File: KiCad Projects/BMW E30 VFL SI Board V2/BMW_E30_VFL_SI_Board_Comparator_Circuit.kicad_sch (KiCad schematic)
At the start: 39 parts, among them K1 SR7-9V-200-1C, Q1 BC547C, U2 LM2901

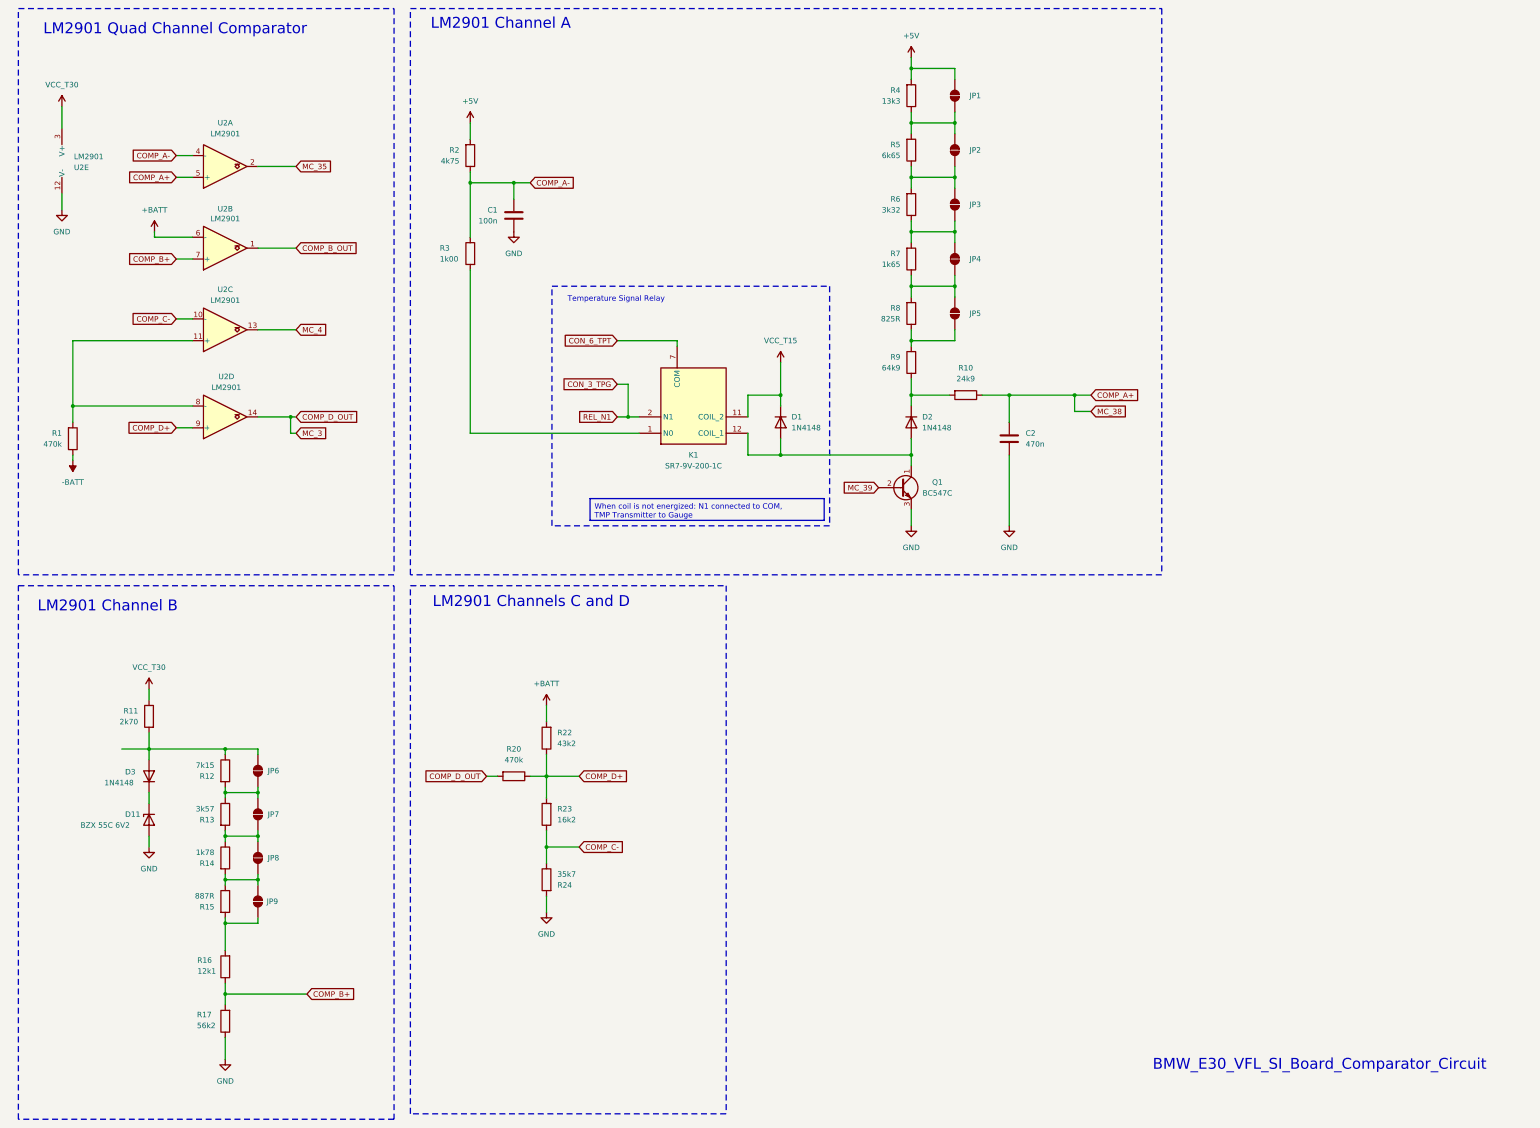
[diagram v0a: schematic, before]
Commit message: Bugfixing of component designators
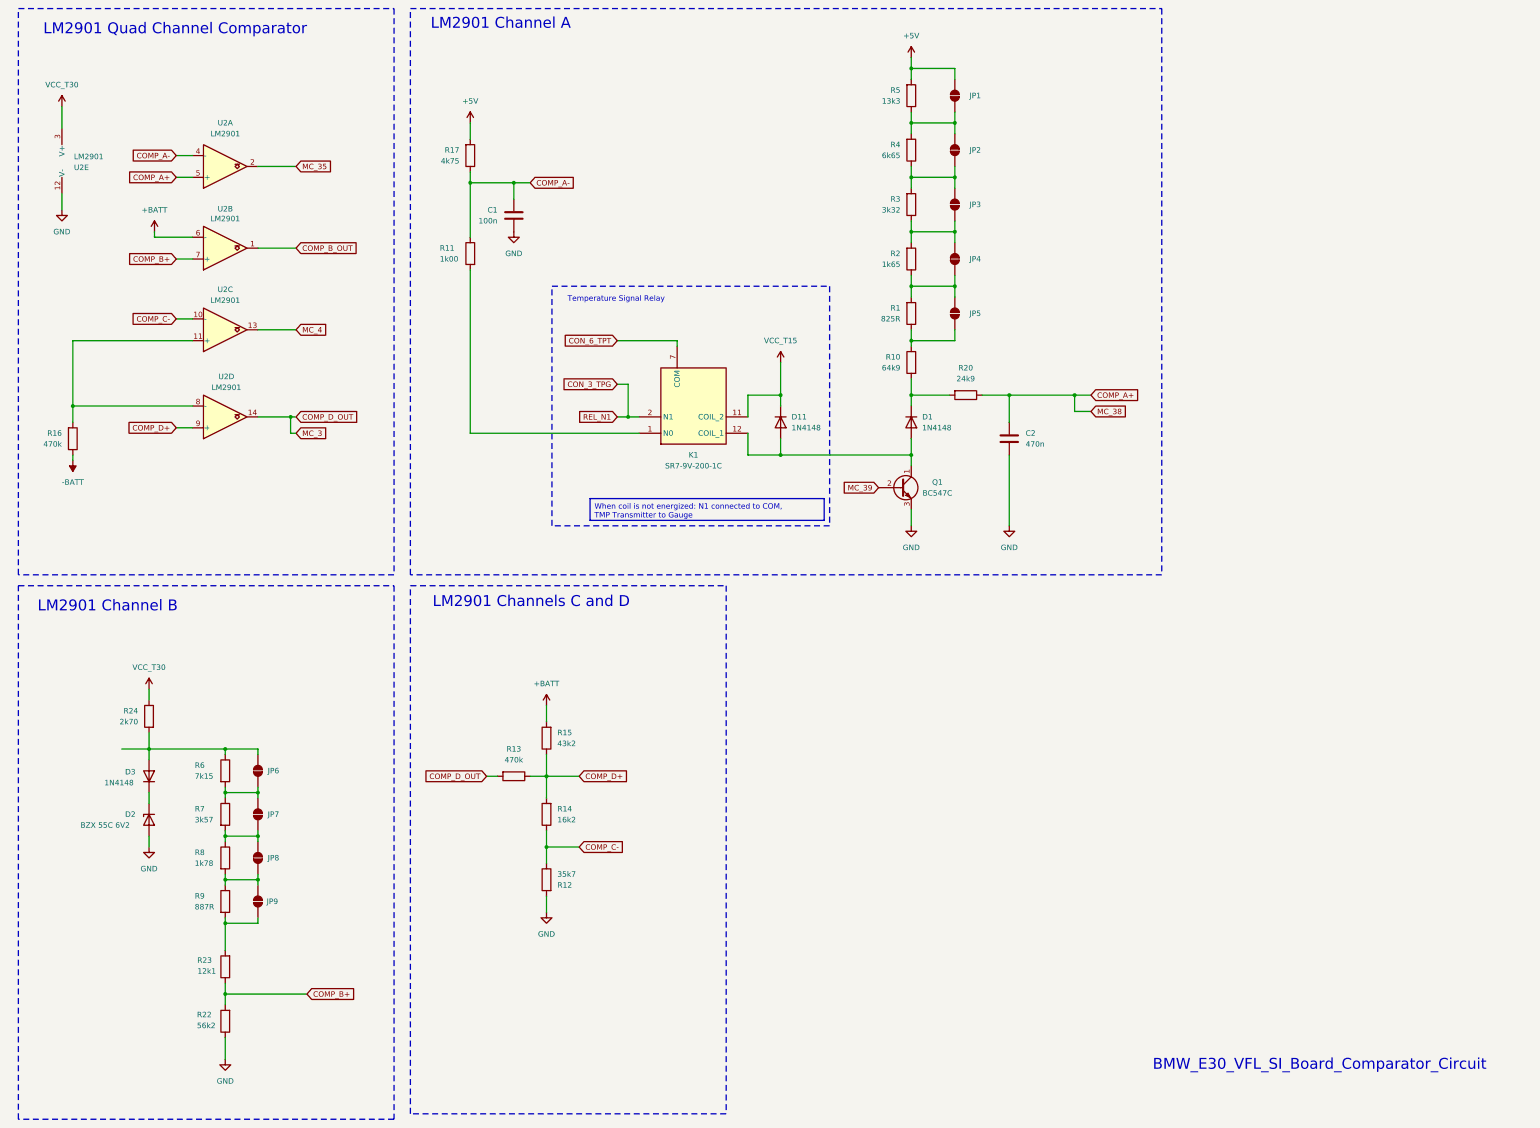
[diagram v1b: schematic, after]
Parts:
- renumbered D2 to D1, D1 to D11, D11 to D2, R8 to R1, R9 to R10, R3 to R11, R24 to R12, R20 to R13, R23 to R14, R22 to R15, R1 to R16, R2 to R17, R7 to R2, R10 to R20, R17 to R22, R16 to R23, R11 to R24, R6 to R3, R5 to R4, R4 to R5, R12 to R6, R13 to R7, R14 to R8, R15 to R9
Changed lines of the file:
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@@
 		(dnp no)
 		(fields_autoplaced yes)
-		(property "Reference" "R5"
+		(property "Reference" "R4"
 			(at 252.73 46.9899 0)
 			(effects
@@
 			(project "BMW E30 VFL SI Board V2"
 				(path "/b9f8b657-f23f-4f46-b33b-c9c07ea00dca/c70e424d-af87-4480-9570-0fdeb437e545"
-					(reference "R5")
+					(reference "R4")
 					(unit 1)
 				)
@@
 		(dnp no)
 		(fields_autoplaced yes)
-		(property "Reference" "D2"
+		(property "Reference" "D1"
 			(at 257.81 110.4899 90)
 			(effects
@@
 			(project "BMW E30 VFL SI Board V2"
 				(path "/b9f8b657-f23f-4f46-b33b-c9c07ea00dca/c70e424d-af87-4480-9570-0fdeb437e545"
-					(reference "D2")
+					(reference "D1")
 					(unit 1)
 				)
@@
 		(on_board yes)
 		(dnp no)
-		(property "Reference" "R24"
+		(property "Reference" "R12"
 			(at 172.72 219.7101 0)
 			(effects
@@
 			(project "BMW E30 VFL SI Board V2"
 				(path "/b9f8b657-f23f-4f46-b33b-c9c07ea00dca/c70e424d-af87-4480-9570-0fdeb437e545"
-					(reference "R24")
+					(reference "R12")
 					(unit 1)
 				)
@@
 		(dnp no)
 		(fields_autoplaced yes)
-		(property "Reference" "R8"
+		(property "Reference" "R1"
 			(at 252.73 85.0899 0)
 			(effects
@@
 			(project "BMW E30 VFL SI Board V2"
 				(path "/b9f8b657-f23f-4f46-b33b-c9c07ea00dca/c70e424d-af87-4480-9570-0fdeb437e545"
-					(reference "R8")
+					(reference "R1")
 					(unit 1)
 				)
@@
 		(dnp no)
 		(fields_autoplaced yes)
-		(property "Reference" "R20"
+		(property "Reference" "R13"
 			(at 162.56 187.96 90)
 			(effects
@@
 			(project "BMW E30 VFL SI Board V2"
 				(path "/b9f8b657-f23f-4f46-b33b-c9c07ea00dca/c70e424d-af87-4480-9570-0fdeb437e545"
-					(reference "R20")
+					(reference "R13")
 					(unit 1)
 				)
@@
 		(dnp no)
 		(fields_autoplaced yes)
-		(property "Reference" "R6"
+		(property "Reference" "R3"
 			(at 252.73 59.6899 0)
 			(effects
@@
 			(project "BMW E30 VFL SI Board V2"
 				(path "/b9f8b657-f23f-4f46-b33b-c9c07ea00dca/c70e424d-af87-4480-9570-0fdeb437e545"
-					(reference "R6")
+					(reference "R3")
 					(unit 1)
 				)
@@
 		(dnp no)
 		(fields_autoplaced yes)
-		(property "Reference" "R22"
+		(property "Reference" "R15"
 			(at 172.72 184.1499 0)
 			(effects
@@
 			(project "BMW E30 VFL SI Board V2"
 				(path "/b9f8b657-f23f-4f46-b33b-c9c07ea00dca/c70e424d-af87-4480-9570-0fdeb437e545"
-					(reference "R22")
+					(reference "R15")
 					(unit 1)
 				)
@@
 		(on_board yes)
 		(dnp no)
-		(property "Reference" "R9"
+		(property "Reference" "R10"
 			(at 252.73 96.5199 0)
 			(effects
@@
 			(project "BMW E30 VFL SI Board V2"
 				(path "/b9f8b657-f23f-4f46-b33b-c9c07ea00dca/c70e424d-af87-4480-9570-0fdeb437e545"
-					(reference "R9")
+					(reference "R10")
 					(unit 1)
 				)
@@
 		(on_board yes)
 		(dnp no)
-		(fields_autoplaced yes)
-		(property "Reference" "R12"
-			(at 92.71 194.3101 0)
+		(property "Reference" "R6"
+			(at 88.138 191.77 0)
 			(effects
 				(font
 					(size 1.27 1.27)
 				)
-				(justify right)
+				(justify left)
 			)
 		)
 		(property "Value" "7k15"
-			(at 92.71 191.7701 0)
+			(at 88.138 194.31 0)
 			(effects
 				(font
 					(size 1.27 1.27)
 				)
-				(justify right)
+				(justify left)
 			)
 		)
@@
 			(project "BMW E30 VFL SI Board V2"
 				(path "/b9f8b657-f23f-4f46-b33b-c9c07ea00dca/c70e424d-af87-4480-9570-0fdeb437e545"
-					(reference "R12")
+					(reference "R6")
 					(unit 1)
 				)
@@
 		(on_board yes)
 		(dnp no)
-		(property "Reference" "R3"
+		(property "Reference" "R11"
 			(at 145.288 71.12 0)
 			(effects
@@
 			(project "BMW E30 VFL SI Board V2"
 				(path "/b9f8b657-f23f-4f46-b33b-c9c07ea00dca/c70e424d-af87-4480-9570-0fdeb437e545"
-					(reference "R3")
+					(reference "R11")
 					(unit 1)
 				)
@@
 		(on_board yes)
 		(dnp no)
-		(fields_autoplaced yes)
-		(property "Reference" "R11"
+		(property "Reference" "R24"
 			(at 74.93 179.0699 0)
 			(effects
@@
 			(project "BMW E30 VFL SI Board V2"
 				(path "/b9f8b657-f23f-4f46-b33b-c9c07ea00dca/c70e424d-af87-4480-9570-0fdeb437e545"
-					(reference "R11")
+					(reference "R24")
 					(unit 1)
 				)
@@
 		(dnp no)
 		(fields_autoplaced yes)
-		(property "Reference" "R23"
+		(property "Reference" "R14"
 			(at 172.72 201.9299 0)
 			(effects
@@
 			(project "BMW E30 VFL SI Board V2"
 				(path "/b9f8b657-f23f-4f46-b33b-c9c07ea00dca/c70e424d-af87-4480-9570-0fdeb437e545"
-					(reference "R23")
+					(reference "R14")
 					(unit 1)
 				)
@@
 		(dnp no)
 		(fields_autoplaced yes)
-		(property "Reference" "R1"
+		(property "Reference" "R16"
 			(at 57.15 114.2999 0)
 			(effects
@@
 			(project "BMW E30 VFL SI Board V2"
 				(path "/b9f8b657-f23f-4f46-b33b-c9c07ea00dca/c70e424d-af87-4480-9570-0fdeb437e545"
-					(reference "R1")
+					(reference "R16")
 					(unit 1)
 				)
@@
 		(on_board yes)
 		(dnp no)
-		(fields_autoplaced yes)
-		(property "Reference" "R13"
-			(at 92.71 204.4701 0)
+		(property "Reference" "R7"
+			(at 88.138 201.93 0)
 			(effects
 				(font
 					(size 1.27 1.27)
 				)
-				(justify right)
+				(justify left)
 			)
 		)
 		(property "Value" "3k57"
-			(at 92.71 201.9301 0)
+			(at 88.138 204.47 0)
 			(effects
 				(font
 					(size 1.27 1.27)
 				)
-				(justify right)
+				(justify left)
 			)
 		)
@@
 			(project "BMW E30 VFL SI Board V2"
 				(path "/b9f8b657-f23f-4f46-b33b-c9c07ea00dca/c70e424d-af87-4480-9570-0fdeb437e545"
-					(reference "R13")
+					(reference "R7")
 					(unit 1)
 				)
@@
 		(dnp no)
 		(fields_autoplaced yes)
-		(property "Reference" "D1"
+		(property "Reference" "D11"
 			(at 227.33 110.4899 90)
 			(effects
@@
 			(project "BMW E30 VFL SI Board V2"
 				(path "/b9f8b657-f23f-4f46-b33b-c9c07ea00dca/c70e424d-af87-4480-9570-0fdeb437e545"
-					(reference "D1")
+					(reference "D11")
 					(unit 1)
 				)
@@
 		(on_board yes)
 		(dnp no)
-		(property "Reference" "R17"
+		(property "Reference" "R22"
 			(at 88.646 249.936 0)
 			(effects
@@
 			(project "BMW E30 VFL SI Board V2"
 				(path "/b9f8b657-f23f-4f46-b33b-c9c07ea00dca/c70e424d-af87-4480-9570-0fdeb437e545"
-					(reference "R17")
+					(reference "R22")
 					(unit 1)
 				)
@@
 		(on_board yes)
 		(dnp no)
-		(property "Reference" "D11"
+		(property "Reference" "D2"
 			(at 71.882 203.2 90)
 			(effects
@@
 			(project "BMW E30 VFL SI Board V2"
 				(path "/b9f8b657-f23f-4f46-b33b-c9c07ea00dca/c70e424d-af87-4480-9570-0fdeb437e545"
-					(reference "D11")
+					(reference "D2")
 					(unit 1)
 				)
@@
 		(dnp no)
 		(fields_autoplaced yes)
-		(property "Reference" "R7"
+		(property "Reference" "R2"
 			(at 252.73 72.3899 0)
 			(effects
@@
 			(project "BMW E30 VFL SI Board V2"
 				(path "/b9f8b657-f23f-4f46-b33b-c9c07ea00dca/c70e424d-af87-4480-9570-0fdeb437e545"
-					(reference "R7")
+					(reference "R2")
 					(unit 1)
 				)
@@
 		(on_board yes)
 		(dnp no)
-		(fields_autoplaced yes)
-		(property "Reference" "R15"
-			(at 92.71 224.7901 0)
+		(property "Reference" "R9"
+			(at 88.138 222.25 0)
 			(effects
 				(font
 					(size 1.27 1.27)
 				)
-				(justify right)
+				(justify left)
 			)
 		)
 		(property "Value" "887R"
-			(at 92.71 222.2501 0)
+			(at 88.138 224.79 0)
 			(effects
 				(font
 					(size 1.27 1.27)
 				)
-				(justify right)
+				(justify left)
 			)
 		)
@@
 			(project "BMW E30 VFL SI Board V2"
 				(path "/b9f8b657-f23f-4f46-b33b-c9c07ea00dca/c70e424d-af87-4480-9570-0fdeb437e545"
-					(reference "R15")
+					(reference "R9")
 					(unit 1)
 				)
@@
 		(dnp no)
 		(fields_autoplaced yes)
-		(property "Reference" "R4"
+		(property "Reference" "R5"
 			(at 252.73 34.2899 0)
 			(effects
@@
 			(project "BMW E30 VFL SI Board V2"
 				(path "/b9f8b657-f23f-4f46-b33b-c9c07ea00dca/c70e424d-af87-4480-9570-0fdeb437e545"
-					(reference "R4")
+					(reference "R5")
 					(unit 1)
 				)
@@
 		(dnp no)
 		(fields_autoplaced yes)
-		(property "Reference" "R2"
+		(property "Reference" "R17"
 			(at 149.86 48.2599 0)
 			(effects
@@
 			(project "BMW E30 VFL SI Board V2"
 				(path "/b9f8b657-f23f-4f46-b33b-c9c07ea00dca/c70e424d-af87-4480-9570-0fdeb437e545"
-					(reference "R2")
+					(reference "R17")
 					(unit 1)
 				)
@@
 		(on_board yes)
 		(dnp no)
-		(property "Reference" "R16"
+		(property "Reference" "R23"
 			(at 90.424 237.236 0)
 			(effects
@@
 			(project "BMW E30 VFL SI Board V2"
 				(path "/b9f8b657-f23f-4f46-b33b-c9c07ea00dca/c70e424d-af87-4480-9570-0fdeb437e545"
-					(reference "R16")
+					(reference "R23")
 					(unit 1)
 				)
@@
 		(on_board yes)
 		(dnp no)
-		(fields_autoplaced yes)
-		(property "Reference" "R14"
-			(at 92.71 214.6301 0)
+		(property "Reference" "R8"
+			(at 88.138 212.09 0)
 			(effects
 				(font
 					(size 1.27 1.27)
 				)
-				(justify right)
+				(justify left)
 			)
 		)
 		(property "Value" "1k78"
-			(at 92.71 212.0901 0)
+			(at 88.138 214.63 0)
 			(effects
 				(font
 					(size 1.27 1.27)
 				)
-				(justify right)
+				(justify left)
 			)
 		)
@@
 			(project "BMW E30 VFL SI Board V2"
 				(path "/b9f8b657-f23f-4f46-b33b-c9c07ea00dca/c70e424d-af87-4480-9570-0fdeb437e545"
-					(reference "R14")
+					(reference "R8")
 					(unit 1)
 				)
@@
 		(dnp no)
 		(fields_autoplaced yes)
-		(property "Reference" "R10"
+		(property "Reference" "R20"
 			(at 267.97 99.06 90)
 			(effects
@@
 			(project "BMW E30 VFL SI Board V2"
 				(path "/b9f8b657-f23f-4f46-b33b-c9c07ea00dca/c70e424d-af87-4480-9570-0fdeb437e545"
-					(reference "R10")
+					(reference "R20")
 					(unit 1)
 				)
